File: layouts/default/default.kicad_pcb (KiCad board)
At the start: 2 copper layers, 28.5 x 38 mm, 40 parts

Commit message: layout done
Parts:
- R3: value 10kΩ ±1% 62.5mW -> 6.2kΩ ±1% 62.5mW; footprint UNI_ROYAL_0402WGF1002TCE:R0402 -> YAGEO_RC0402FR_076K2L:R0402
- R4: value 16kΩ ±1% 62.5mW -> 10kΩ ±1% 62.5mW; footprint UNI_ROYAL_0402WGF1602TCE:R0402 -> UNI_ROYAL_0402WGF1002TCE:R0402
- moved B1 1.05 mm to (129.7, 98.2)
- moved C10 0.08 mm to (131.4, 100.1)
- moved C11 0.08 mm to (128.8, 100.1)
- moved C9 0.07 mm to (133.2, 98.8)
- moved R11 0.07 mm to (127.2, 98.5)
- moved R12 0.07 mm to (133.2, 97.6)
- moved R13 0.07 mm to (127.2, 97.5)
- moved U5 0.07 mm to (130.2, 98.2)
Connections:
- C3 pad 2: output-1 -> output-0
- C4 pad 2: output-0 -> output-1
- Card1 pad 2: output-1 -> CD_DAT3
- R7 pad 2: output-0 -> output-1
- SW1 pad 3: output-1 -> output-0
- SW1 pad 4: output-1 -> output-0
- SW2 pad 3: output-0 -> output-1
- SW2 pad 4: output-0 -> output-1
- U2 pad 18: mcu-line-1 -> CD_DAT3
- U2 pad 23: output-1 -> output-0
- U2 pad 26: mcu-line-2 -> mcu-line-1
- U2 pad 27: mcu-line-3 -> mcu-line-2
- U2 pad 30: mcu-line-4 -> mcu-line-3
- U2 pad 31: mcu-line-5 -> mcu-line-4
- U2 pad 8: output-0 -> output-1
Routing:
- net hv-1: track 24.3 -> 52.2 mm, vias 5 -> 7
- net CD_DAT3: track 0.00 -> 13.1 mm
- net output-1: track 6.52 -> 9.53 mm
- net output-0: track 9.53 -> 6.52 mm, vias 0 -> 1
- net -hv-0: track 39.4 -> 40.1 mm
- net gnd: vias 6 -> 7

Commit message: add nice logo
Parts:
- added LOGO1: , atopile_Logo_4x4mm:atopile_Logo_4x4mm, F.Cu at (118.4, 78.1)
- moved R8 3.64 mm to (122.8, 83.6), turned to -90 degrees
- moved C7 2.74 mm to (121.8, 83.4), turned to -90 degrees
- moved U3 2.68 mm to (122.7, 80.3), turned to 90 degrees
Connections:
- Card1 pad 2: CD_DAT3 -> line-4
- Card1 pad 5: line-4 -> line-5
- Card1 pad 7: line-5 -> line-6
- Card1 pad 8: line-6 -> line-7
- D1 pad 1: line-7 -> line-8
- D1 pad 3: line-8 -> line-9
- D1 pad 4: line-8 -> line-9
- D1 pad 6: line-7 -> line-8
- R14 pad 1: line-5 -> line-6
- R15 pad 1: line-6 -> line-7
- R16 pad 1: line-4 -> line-5
- R6 pad 1: line-5 -> line-6
- U2 pad 16: line-4 -> line-5
- U2 pad 18: CD_DAT3 -> line-4
- U2 pad 21: line-6 -> line-7
- U2 pad 22: line-5 -> line-6
- USB1 pad 5: line-7 -> line-8
- USB1 pad 6: line-8 -> line-9
- USB1 pad 7: line-7 -> line-8
- USB1 pad 8: line-8 -> line-9
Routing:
- net line-7: track 7.57 -> 24.5 mm, vias 0 -> 2
- net line-4: track 26.6 -> 13.1 mm, vias 2 -> 0
- net CD_DAT3: track 13.1 -> 0.00 mm
- net line-9: track 0.00 -> 6.68 mm
- net -line-3: track 21.1 -> 16.9 mm
- net -line-4: track 14.8 -> 11.9 mm
- net line-6: track 24.5 -> 27.2 mm
- net gnd: track 30.6 -> 32.1 mm
- net -line-2: track 20.4 -> 19.5 mm
- net line-8: track 6.68 -> 7.57 mm
- net line-5: track 27.2 -> 26.6 mm
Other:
- board size 28.5 x 38 mm -> 28.8 x 41.5 mm

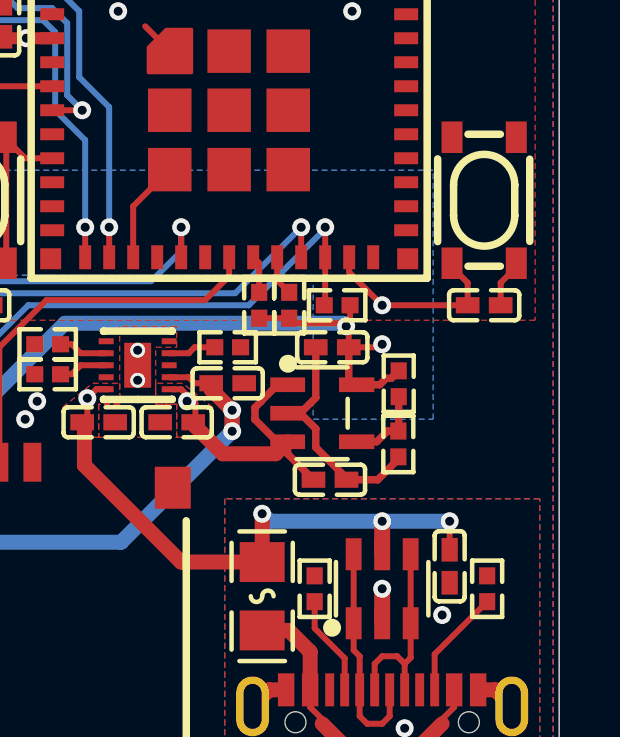
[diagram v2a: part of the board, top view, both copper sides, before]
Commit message: fix add usb comms connection
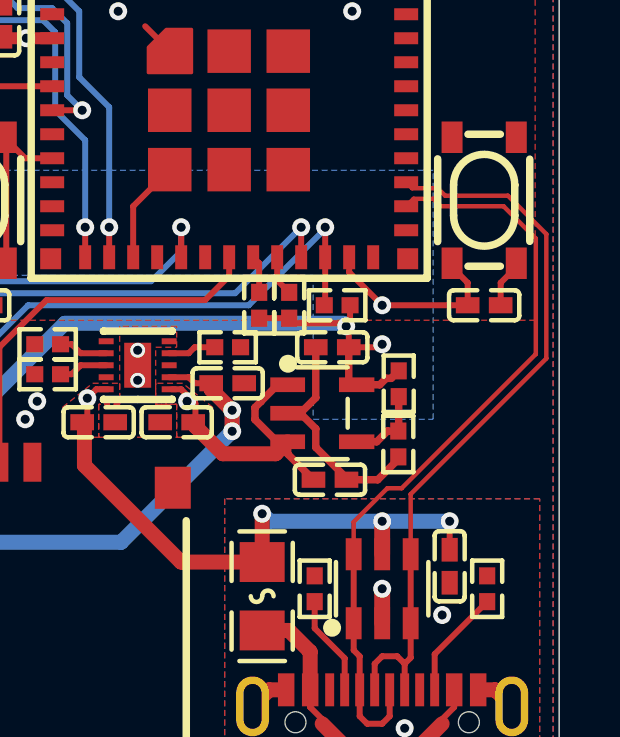
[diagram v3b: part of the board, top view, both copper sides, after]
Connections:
- U2 pad 26: mcu-line-1 -> line-8
- U2 pad 27: mcu-line-2 -> line-9
- U2 pad 30: mcu-line-3 -> mcu-line-1
- U2 pad 31: mcu-line-4 -> mcu-line-2
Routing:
- net line-8: track 7.57 -> 25.9 mm
- net line-9: track 6.68 -> 24.6 mm

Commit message: looking good
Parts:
- added C13: 100nF ±10% 16V X7R, Samsung_Electro_Mechanics_CL05B104KO5NNNC:C0402, F.Cu at (141.9, 79.6)
- added LED1: , OPSCO_Optoelectronics_SK6805_EC20:LED-SMD_4P-L2.0-W2.0-BR, F.Cu at (141.8, 77.5)
- added LED3: , Hubei_KENTO_Elec_KT_0603R:LED0603-RD, F.Cu at (142.8, 86.1)
- added R17: 10kΩ ±1% 62.5mW, UNI_ROYAL_0402WGF1002TCE:R0402, F.Cu at (128.7, 96.5)
- added R19: 10kΩ ±1% 62.5mW, UNI_ROYAL_0402WGF1002TCE:R0402, F.Cu at (142.8, 88.7)
- R3: value 6.2kΩ ±1% 62.5mW -> 10kΩ ±1% 62.5mW; footprint YAGEO_RC0402FR_076K2L:R0402 -> UNI_ROYAL_0402WGF1002TCE:R0402
- R4: value 10kΩ ±1% 62.5mW -> 16kΩ ±1% 62.5mW; footprint UNI_ROYAL_0402WGF1002TCE:R0402 -> UNI_ROYAL_0402WGF1602TCE:R0402
- moved R15 5.50 mm to (124.4, 99.2)
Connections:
- net line-6 renamed sd_miso
- net mcu-line-0 renamed mcu-line
- Card1 pad 2: line-4 -> sd_chip_select_1
- Card1 pad 3: CMD -> sd_mosi
- Card1 pad 5: line-5 -> sd_clk
- Card1 pad 8: line-7 -> DAT1
- D1 pad 1: line-8 -> line-4
- D1 pad 3: line-9 -> line-5
- D1 pad 4: line-9 -> line-5
- D1 pad 6: line-8 -> line-4
- R1 pad 2: -line-0 -> -line-1
- R15 pad 1: line-7 -> sd_mosi
- R16 pad 1: line-5 -> sd_clk
- R2 pad 2: -line-1 -> -line-2
- R8 pad 1: -line-3 -> -line-4
- U2 pad 12: -line-2 -> -line-3
- U2 pad 13: -line-3 -> -line-4
- U2 pad 16: line-5 -> sd_clk
- U2 pad 18: line-4 -> sd_chip_select_1
- U2 pad 19: -line-0 -> -line-1
- U2 pad 20: -line-1 -> -line-2
- U2 pad 21: line-7 -> sd_mosi
- U2 pad 26: line-8 -> line-4
- U2 pad 27: line-9 -> line-5
- U2 pad 30: mcu-line-1 -> anode
- U2 pad 31: mcu-line-2 -> -line-0
- U2 pad 6: -line-4 -> -line-5
- U3 pad 1: -line-4 -> -line-5
- U3 pad 4: -line-2 -> -line-3
- U3 pad 6: -line-3 -> -line-4
- USB1 pad 5: line-8 -> line-4
- USB1 pad 6: line-9 -> line-5
- USB1 pad 7: line-8 -> line-4
- USB1 pad 8: line-9 -> line-5
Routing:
- net hv-1: track 52.2 -> 91.4 mm, vias 7 -> 8
- net gnd: track 32.1 -> 63.2 mm, vias 7 -> 17
- net sd_mosi: track 0.00 -> 28.7 mm, vias 0 -> 2
- net line-8: track 25.9 -> 0.00 mm
- net sd_clk: track 0.00 -> 25.1 mm, vias 0 -> 2
- net line-9: track 24.6 -> 0.00 mm
- net line-7: track 24.5 -> 0.00 mm, vias 2 -> 0
- net -line-2: track 19.5 -> 1.34 mm, vias 2 -> 0
- net sd_chip_select_1: track 0.00 -> 13.9 mm
- net line-4: track 13.1 -> 25.9 mm
- net -line-5: track 0.00 -> 11.9 mm, vias 0 -> 2
- net -line-0: track 1.25 -> 12.5 mm
- net anode: track 0.00 -> 6.28 mm
- net -line-4: track 11.9 -> 16.7 mm
- net -line-3: track 16.9 -> 19.5 mm
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
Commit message: cleaning up readme
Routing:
- net DAT1: track 1.30 -> 0.00 mm
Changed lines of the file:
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@@
 			(layer "F.Fab")
 		)
-		(fp_text user "${REFERENCE}"
-			(at 0 0 180)
-			(layer "F.Fab")
-			(effects
-				(font
-					(size 1 1)
-					(thickness 0.15)
-				)
-			)
-		)
 		(pad "1" smd rect
 			(at -0.55 0 180)
@@
 			(layer "F.Fab")
 		)
-		(fp_text user "${REFERENCE}"
-			(at 0 0 0)
-			(layer "F.Fab")
-			(effects
-				(font
-					(size 1 1)
-					(thickness 0.15)
-				)
-			)
-		)
 		(pad "1" smd rect
 			(at -0.43 0 270)
@@
 			(layer "F.Fab")
 		)
-		(fp_text user "${REFERENCE}"
-			(at 0 0 0)
-			(layer "F.Fab")
-			(effects
-				(font
-					(size 1 1)
-					(thickness 0.15)
-				)
-			)
-		)
 		(pad "1" smd rect
 			(at -0.43 0 270)
@@
 			(layer "F.Fab")
 		)
-		(fp_text user "${REFERENCE}"
-			(at 0 0 0)
-			(layer "F.Fab")
-			(effects
-				(font
-					(size 1 1)
-					(thickness 0.15)
-				)
-			)
-		)
 		(pad "1" smd rect
 			(at -0.43 0)
@@
 			(layer "F.Fab")
 		)
-		(fp_text user "${REFERENCE}"
-			(at 0 0 0)
-			(layer "F.Fab")
-			(effects
-				(font
-					(size 1 1)
-					(thickness 0.15)
-				)
-			)
-		)
 		(pad "1" smd rect
 			(at 0.65 0.65)
@@
 	)
 	(segment
-		(start 119 102.2)
-		(end 119 102.5)
-		(width 0.2)
-		(layer "F.Cu")
-		(net 30)
-	)
-	(segment
-		(start 119 101.2)
-		(end 119 102.2)
-		(width 0.2)
-		(layer "F.Cu")
-		(net 30)
-	)
-	(segment
